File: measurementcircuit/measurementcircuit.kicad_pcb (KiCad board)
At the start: 2 copper layers, 174.5 x 220 mm, 81 parts, among them J1 Conn_01x02, J10 Conn_01x02, J11 Conn_01x02, J12 Conn_01x02, J13 250-108/000-006, J15 Conn_01x02, J16 Conn_01x02, J17 250-116/000-012, J18 2604-3102, J19 2604-3102, J2 Conn_01x02, J20 2604-3102, J21 Conn_01x02, J22 Conn_01x02, J23 Conn_01x02, J24 Conn_01x02, J25 Conn_01x02, J26 Conn_01x02, J27 Conn_01x02, J28 Conn_01x02, J29 Conn_01x02, J3 2604-3102, J30 Conn_01x02, J31 Conn_01x02, J32 Conn_01x02, J33 Conn_01x02, J34 Conn_01x02, J35 Conn_01x02, J36 Conn_01x02, J37 Conn_01x02, J38 Conn_01x02, J39 Conn_01x02, J4 2604-3102, J40 Conn_01x02, J41 Conn_01x02, J42 Conn_01x02, J5 2604-3102, J6 2604-3102, J7 2604-3102, J8 Conn_01x02, J9 Conn_01x02

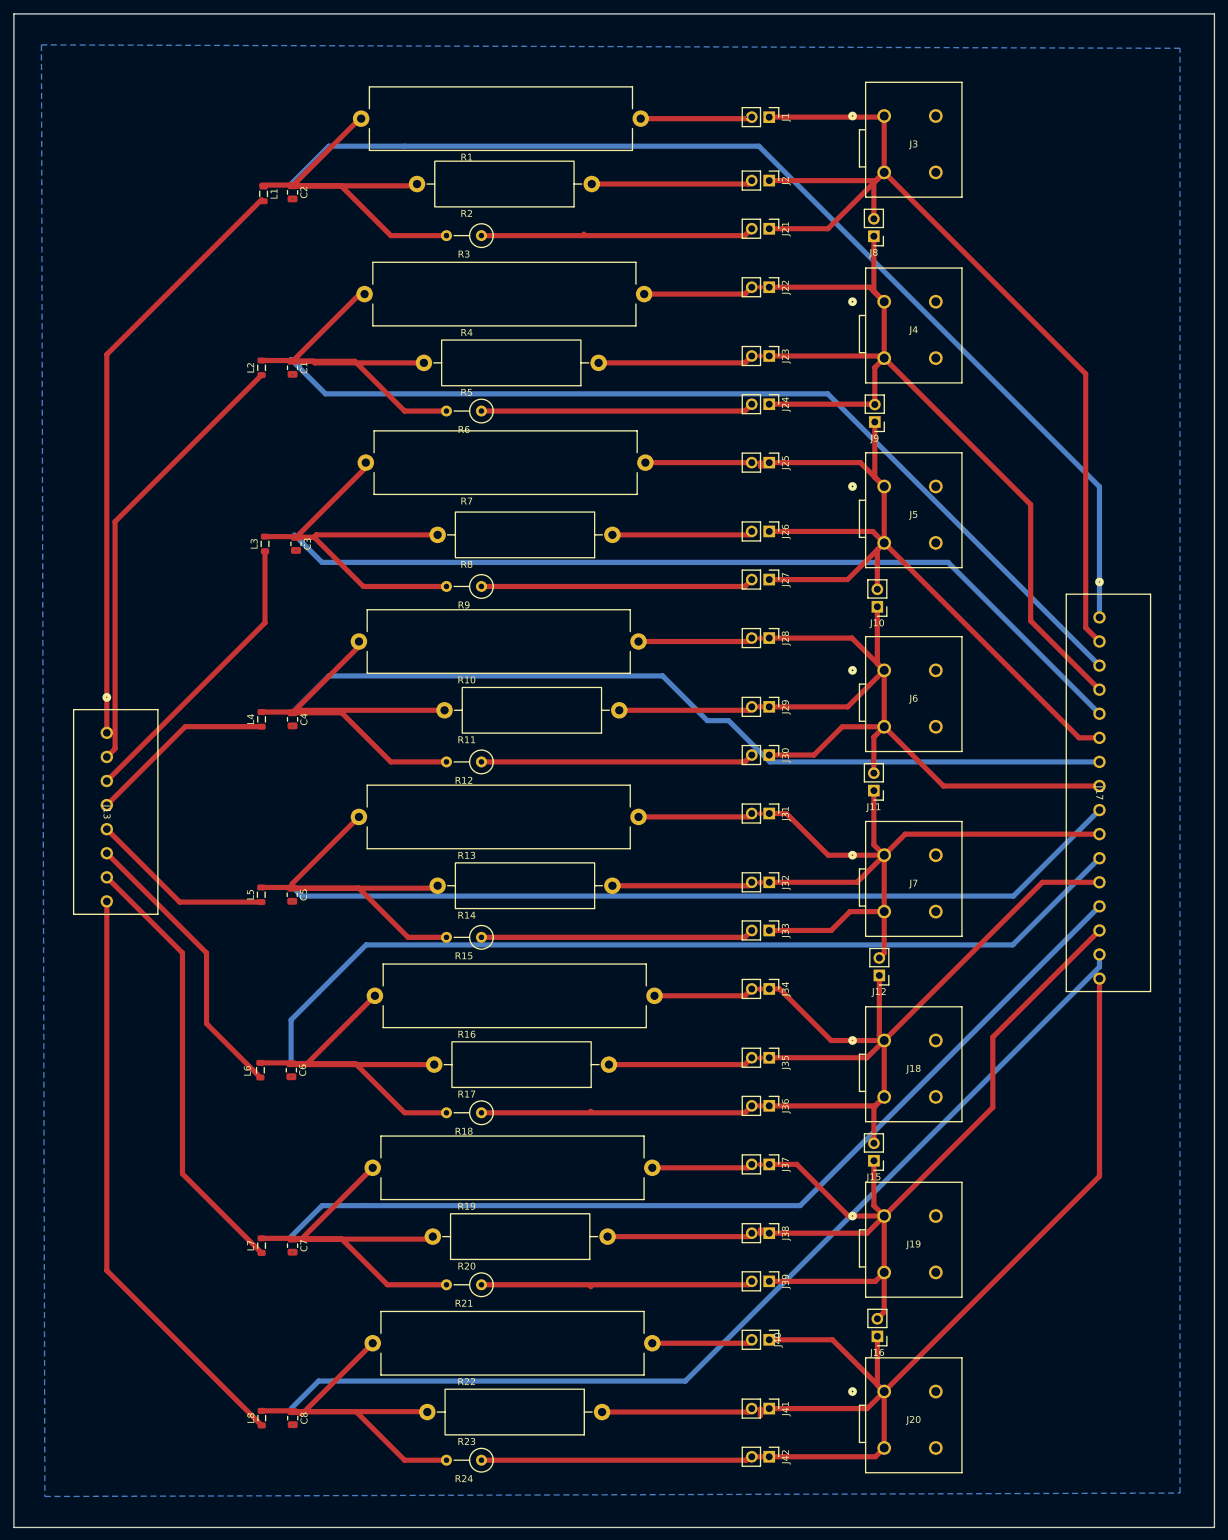
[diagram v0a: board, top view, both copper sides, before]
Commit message: First Redesign Changes
Switch to 4-layer PCB with inner copper layers as ground layers for top and bottom. Add holes for standoffs. Clockwise orientation of schematic to accommodate double the channels.
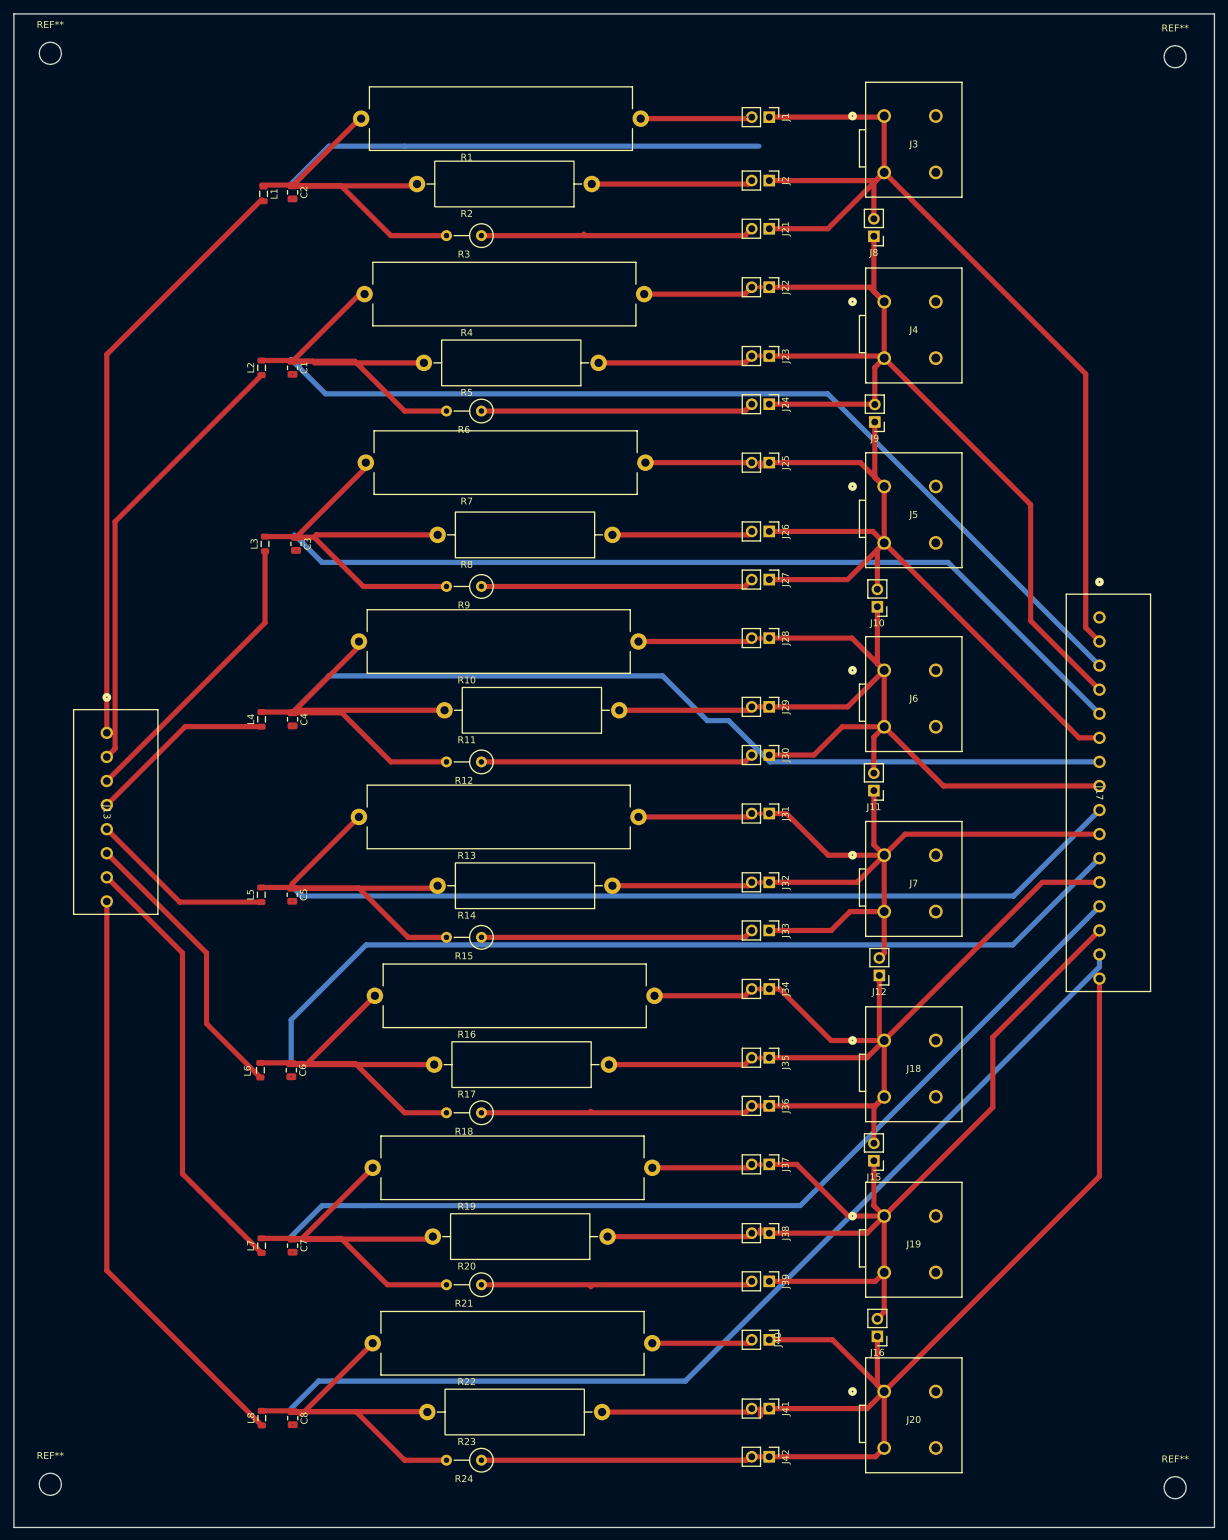
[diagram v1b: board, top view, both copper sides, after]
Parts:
- added REF**: MountingHole_3.2mm_M3, MountingHole:MountingHole_3.2mm_M3, F.Cu at (-26.5, 135.0)
- added REF**: MountingHole_3.2mm_M3, MountingHole:MountingHole_3.2mm_M3, F.Cu at (-26.5, -73.0)
- added REF**: MountingHole_3.2mm_M3, MountingHole:MountingHole_3.2mm_M3, F.Cu at (-190.0, -73.5)
- added REF**: MountingHole_3.2mm_M3, MountingHole:MountingHole_3.2mm_M3, F.Cu at (-190.0, 134.5)
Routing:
- net Net-(C2-Pad1): track 221.6 -> 132.6 mm
- added copper zone on In1.Cu, net GND
- added copper zone on In2.Cu, net GND
- removed copper zone on B.Cu, net GND
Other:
- copper layers 2 -> 4

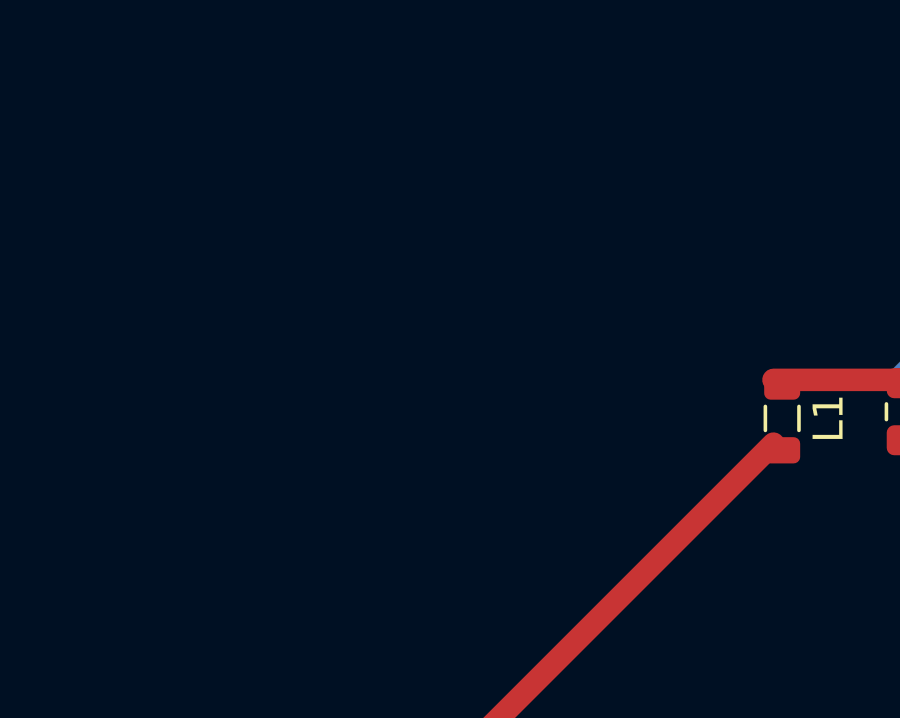
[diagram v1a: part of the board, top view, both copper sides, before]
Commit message: Redesign Work - Symbols, Schematic Overhaul
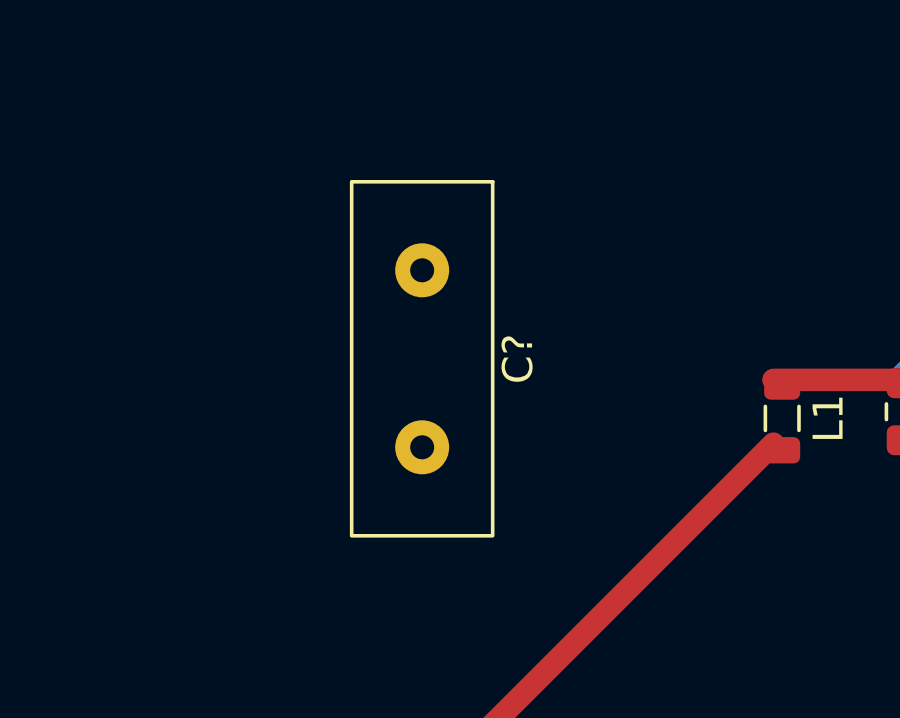
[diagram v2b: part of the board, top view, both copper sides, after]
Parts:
- added C?: 10pF, 10pF_Capacitor_Custom:C_Disc_Radial_P5.90mm_W4.3mm_L11.4mm_Placeholder, F.Cu at (-171.0, -58.0)
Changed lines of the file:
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@@
 		)
+	)
+	(footprint "10pF_Capacitor_Custom:C_Disc_Radial_P5.90mm_W4.3mm_L11.4mm_Placeholder"
+		(layer "F.Cu")
+		(at -171 -58 -90)
+		(descr "Placeholder: Cornell Dubilier CD17 series style mica cap, THT, 5.90mm pitch, body ~11.4x4.3mm")
+		(tags "capacitor THT radial mica placeholder P5.90mm")
+		(property "Reference" "C?"
+			(at 2.95 -3.2 90)
+			(layer "F.SilkS")
+			(effects
+				(font
+					(size 1 1)
+					(thickness 0.15)
+				)
+			)
+		)
+		(property "Value" "10pF"
+			(at 2.95 3.2 90)
+			(layer "F.Fab")
+			(effects
+				(font
+					(size 1 1)
+					(thickness 0.15)
+				)
+			)
+		)
+		(property "Datasheet" ""
+			(at 0 0 90)
+			(layer "F.Fab")
+			(hide yes)
+			(effects
+				(font
+					(size 1.27 1.27)
+					(thickness 0.15)
+				)
+			)
+		)
+		(property "Description" ""
+			(at 0 0 90)
+			(layer "F.Fab")
+			(hide yes)
+			(effects
+				(font
+					(size 1.27 1.27)
+					(thickness 0.15)
+				)
+			)
+		)
+		(attr through_hole)
+		(fp_rect
+			(start -2.95 -2.35)
+			(end 8.85 2.35)
+			(stroke
+				(width 0.12)
+				(type solid)
+			)
+			(fill no)
+			(layer "F.SilkS")
+		)
+		(fp_rect
+			(start -3.45 -2.85)
+			(end 9.35 2.85)
+			(stroke
+				(width 0.05)
+				(type solid)
+			)
+			(fill no)
+			(layer "F.CrtYd")
+		)
+		(fp_rect
+			(start -2.75 -2.15)
+			(end 8.65 2.15)
+			(stroke
+				(width 0.1)
+				(type solid)
+			)
+			(fill no)
+			(layer "F.Fab")
+		)
+		(fp_text user "${REFERENCE}"
+			(at 2.95 0 90)
+			(layer "F.Fab")
+			(effects
+				(font
+					(size 1 1)
+					(thickness 0.12)
+				)
+			)
+		)
+		(pad "1" thru_hole circle
+			(at 0 0 270)
+			(size 1.8 1.8)
+			(drill 0.8)
+			(layers "*.Cu" "*.Mask")
+			(remove_unused_layers no)
+		)
+		(pad "2" thru_hole circle
+			(at 5.9 0 270)
+			(size 1.8 1.8)
+			(drill 0.8)
+			(layers "*.Cu" "*.Mask")
+			(remove_unused_layers no)
+		)
+		(embedded_fonts no)
 	)
 	(footprint "Resistor_THT:R_Axial_Power_L20.0mm_W6.4mm_P25.40mm"

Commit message: Figured out Bottom layer placement, some footprint changes
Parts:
- removed C?: 10pF, 10pF_Capacitor_Custom:C_Disc_Radial_P5.90mm_W4.3mm_L11.4mm_Placeholder
- removed REF** (x4): MountingHole_3.2mm_M3, MountingHole:MountingHole_3.2mm_M3
- added C11: 10pF, Capacitor_SMD:C_0805_2012Metric, B.Cu at (48.4, -4.12)
- added C12: 10pF, Capacitor_SMD:C_0805_2012Metric, B.Cu at (48.4, -1.11)
- added C13: 10pF, Capacitor_SMD:C_0805_2012Metric, B.Cu at (48.4, 1.90)
- added C14: 10pF, Capacitor_SMD:C_0805_2012Metric, B.Cu at (48.4, 4.91)
- added C15: 10pF, Capacitor_SMD:C_0805_2012Metric, B.Cu at (48.4, 7.92)
- added C16: 10pF, Capacitor_SMD:C_0805_2012Metric, B.Cu at (48.4, 10.9)
- added C18: 10pF, Capacitor_SMD:C_0805_2012Metric, B.Cu at (48.4, 13.9)
- added J47: Conn_01x02, Connector_PinHeader_2.54mm:PinHeader_1x02_P2.54mm_Vertical, B.Cu at (80.5, -3.33)
- added J48: Conn_01x02, Connector_PinHeader_2.54mm:PinHeader_1x02_P2.54mm_Vertical, B.Cu at (75.9, -3.33)
- added J49: Conn_01x02, Connector_PinHeader_2.54mm:PinHeader_1x02_P2.54mm_Vertical, B.Cu at (71.3, -3.33)
- added J51: Conn_01x02, Connector_PinHeader_2.54mm:PinHeader_1x02_P2.54mm_Vertical, B.Cu at (66.7, -3.33)
- added J52: Conn_01x02, Connector_PinHeader_2.54mm:PinHeader_1x02_P2.54mm_Vertical, B.Cu at (62.1, -3.33)
- added J53: Conn_01x02, Connector_PinHeader_2.54mm:PinHeader_1x02_P2.54mm_Vertical, B.Cu at (57.5, -3.33)
- added J54: Conn_01x02, Connector_PinHeader_2.54mm:PinHeader_1x02_P2.54mm_Vertical, B.Cu at (80.5, 3.81)
- added J56: Conn_01x02, Connector_PinHeader_2.54mm:PinHeader_1x02_P2.54mm_Vertical, B.Cu at (75.9, 3.81)
- added J57: Conn_01x02, Connector_PinHeader_2.54mm:PinHeader_1x02_P2.54mm_Vertical, B.Cu at (71.3, 3.81)
- added J58: Conn_01x02, Connector_PinHeader_2.54mm:PinHeader_1x02_P2.54mm_Vertical, B.Cu at (66.7, 3.81)
- added J59: Conn_01x02, Connector_PinHeader_2.54mm:PinHeader_1x02_P2.54mm_Vertical, B.Cu at (62.1, 3.81)
- added J62: Conn_01x02, Connector_PinHeader_2.54mm:PinHeader_1x02_P2.54mm_Vertical, B.Cu at (57.5, 3.81)
- added J63: Conn_01x02, Connector_PinHeader_2.54mm:PinHeader_1x02_P2.54mm_Vertical, B.Cu at (80.5, 10.9)
- added J64: Conn_01x02, Connector_PinHeader_2.54mm:PinHeader_1x02_P2.54mm_Vertical, B.Cu at (75.9, 10.9)
- added J65: Conn_01x02, Connector_PinHeader_2.54mm:PinHeader_1x02_P2.54mm_Vertical, B.Cu at (71.3, 10.9)
- added J67: Conn_01x02, Connector_PinHeader_2.54mm:PinHeader_1x02_P2.54mm_Vertical, B.Cu at (66.7, 10.9)
- added J68: Conn_01x02, Connector_PinHeader_2.54mm:PinHeader_1x02_P2.54mm_Vertical, B.Cu at (62.1, 10.9)
- added J69: Conn_01x02, Connector_PinHeader_2.54mm:PinHeader_1x02_P2.54mm_Vertical, B.Cu at (57.5, 10.9)
- added J70: Conn_01x02, Connector_PinHeader_2.54mm:PinHeader_1x02_P2.54mm_Vertical, B.Cu at (80.5, 18.1)
- added J72: Conn_01x02, Connector_PinHeader_2.54mm:PinHeader_1x02_P2.54mm_Vertical, B.Cu at (75.9, 18.1)
- added J73: Conn_01x02, Connector_PinHeader_2.54mm:PinHeader_1x02_P2.54mm_Vertical, B.Cu at (71.3, 18.1)
- added J74: Conn_01x02, Connector_PinHeader_2.54mm:PinHeader_1x02_P2.54mm_Vertical, B.Cu at (66.7, 18.1)
- added J75: Conn_01x02, Connector_PinHeader_2.54mm:PinHeader_1x02_P2.54mm_Vertical, B.Cu at (62.1, 18.1)
- added J77: Conn_01x02, Connector_PinHeader_2.54mm:PinHeader_1x02_P2.54mm_Vertical, B.Cu at (57.5, 18.1)
- added J78: Conn_01x02, Connector_PinHeader_2.54mm:PinHeader_1x02_P2.54mm_Vertical, B.Cu at (80.5, 25.2)
- added J79: Conn_01x02, Connector_PinHeader_2.54mm:PinHeader_1x02_P2.54mm_Vertical, B.Cu at (75.9, 25.2)
- added J80: Conn_01x02, Connector_PinHeader_2.54mm:PinHeader_1x02_P2.54mm_Vertical, B.Cu at (71.3, 25.2)
- added J82: Conn_01x02, Connector_PinHeader_2.54mm:PinHeader_1x02_P2.54mm_Vertical, B.Cu at (66.7, 25.2)
- added J83: Conn_01x02, Connector_PinHeader_2.54mm:PinHeader_1x02_P2.54mm_Vertical, B.Cu at (62.1, 25.2)
- added J84: Conn_01x02, Connector_PinHeader_2.54mm:PinHeader_1x02_P2.54mm_Vertical, B.Cu at (57.5, 25.2)
- added L10: 56μH, Inductor_SMD:L_0805_2012Metric, B.Cu at (52.9, -1.50)
- added L11: 56μH, Inductor_SMD:L_0805_2012Metric, B.Cu at (52.9, 1.25)
- added L12: 56μH, Inductor_SMD:L_0805_2012Metric, B.Cu at (52.9, 4.00)
- added L13: 56μH, Inductor_SMD:L_0805_2012Metric, B.Cu at (52.9, 6.75)
- added L14: 56μH, Inductor_SMD:L_0805_2012Metric, B.Cu at (52.9, 9.49)
- added L15: 56μH, Inductor_SMD:L_0805_2012Metric, B.Cu at (52.9, 12.2)
- added L16: 56μH, Inductor_SMD:L_0805_2012Metric, B.Cu at (52.9, 15.0)
- added L9: 56μH, Inductor_SMD:L_0805_2012Metric, B.Cu at (52.9, -4.25)
- added R25: 10 Ohm, Resistor_THT:R_Axial_Power_L38.0mm_W9.0mm_P40.64mm, B.Cu at (4.64, -64.0)
- added R26: 50 Ohm, Resistor_THT:R_Axial_Power_L20.0mm_W6.4mm_P25.40mm, B.Cu at (80.8, -65.3)
- added R27: 500 Ohm, Resistor_THT:R_Axial_DIN0309_L9.0mm_D3.2mm_P5.08mm_Vertical, B.Cu at (51.0, -66.9)
- added R28: 10 Ohm, Resistor_THT:R_Axial_Power_L38.0mm_W9.0mm_P40.64mm, B.Cu at (45.3, -53.4)
- added R29: 50 Ohm, Resistor_THT:R_Axial_Power_L20.0mm_W6.4mm_P25.40mm, B.Cu at (80.8, -57.3)
- added R30: 500 Ohm, Resistor_THT:R_Axial_DIN0309_L9.0mm_D3.2mm_P5.08mm_Vertical, B.Cu at (51.0, -62.1)
- added R31: 10 Ohm, Resistor_THT:R_Axial_Power_L38.0mm_W9.0mm_P40.64mm, B.Cu at (45.3, -42.9)
- added R32: 50 Ohm, Resistor_THT:R_Axial_Power_L20.0mm_W6.4mm_P25.40mm, B.Cu at (80.8, -49.4)
- added R33: 500 Ohm, Resistor_THT:R_Axial_DIN0309_L9.0mm_D3.2mm_P5.08mm_Vertical, B.Cu at (51.0, -57.4)
- added R34: 10 Ohm, Resistor_THT:R_Axial_Power_L38.0mm_W9.0mm_P40.64mm, B.Cu at (45.3, -32.3)
- added R35: 50 Ohm, Resistor_THT:R_Axial_Power_L20.0mm_W6.4mm_P25.40mm, B.Cu at (80.8, -41.4)
- added R36: 500 Ohm, Resistor_THT:R_Axial_DIN0309_L9.0mm_D3.2mm_P5.08mm_Vertical, B.Cu at (51.0, -52.6)
- added R37: 10 Ohm, Resistor_THT:R_Axial_Power_L38.0mm_W9.0mm_P40.64mm, B.Cu at (45.3, -21.8)
- added R38: 50 Ohm, Resistor_THT:R_Axial_Power_L20.0mm_W6.4mm_P25.40mm, B.Cu at (80.8, -33.5)
- added R39: 500 Ohm, Resistor_THT:R_Axial_DIN0309_L9.0mm_D3.2mm_P5.08mm_Vertical, B.Cu at (51.0, -47.9)
- added R40: 10 Ohm, Resistor_THT:R_Axial_Power_L38.0mm_W9.0mm_P40.64mm, B.Cu at (45.3, -11.2)
- added R41: 50 Ohm, Resistor_THT:R_Axial_Power_L20.0mm_W6.4mm_P25.40mm, B.Cu at (80.8, -25.5)
- added R42: 500 Ohm, Resistor_THT:R_Axial_DIN0309_L9.0mm_D3.2mm_P5.08mm_Vertical, B.Cu at (51.0, -43.1)
- added R43: 10 Ohm, Resistor_THT:R_Axial_Power_L38.0mm_W9.0mm_P40.64mm, B.Cu at (45.3, -0.66)
- added R44: 50 Ohm, Resistor_THT:R_Axial_Power_L20.0mm_W6.4mm_P25.40mm, B.Cu at (80.8, -17.6)
- added R45: 500 Ohm, Resistor_THT:R_Axial_DIN0309_L9.0mm_D3.2mm_P5.08mm_Vertical, B.Cu at (51.0, -38.4)
- added R46: 10 Ohm, Resistor_THT:R_Axial_Power_L38.0mm_W9.0mm_P40.64mm, B.Cu at (45.3, 9.89)
- added R47: 50 Ohm, Resistor_THT:R_Axial_Power_L20.0mm_W6.4mm_P25.40mm, B.Cu at (80.8, -9.61)
- added R48: 500 Ohm, Resistor_THT:R_Axial_DIN0309_L9.0mm_D3.2mm_P5.08mm_Vertical, B.Cu at (51.0, -33.6)
- J13: value 250-108/000-006 -> 2604-3102
- J17: value 250-116/000-012 -> Conn_01x02; footprint Senior_Design:CONN16_250-116&slash_000-012_WAG -> Connector_PinHeader_2.54mm:PinHeader_1x02_P2.54mm_Vertical
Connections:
- C1 pad 1: Net-(J22-Pin_1) -> Net-(J4-1_1)
- C4 pad 1: Net-(J10-Pin_1) -> Net-(C4-Pad1)
- J13 pad 1: Net-(J13-Pad1) -> Net-(J13-1_1)
- J13 pad 2: Net-(J13-Pad2) -> Net-(J13-1_1)
- J13 pad 3: Net-(J13-Pad3) -> GND
- J13 pad 4: Net-(J13-Pad4) -> GND
- J13 pad 5: Net-(J13-Pad5) -> (no net)
- J13 pad 6: Net-(J13-Pad6) -> (no net)
- J13 pad 7: Net-(J13-Pad7) -> (no net)
- J13 pad 8: Net-(J13-Pad8) -> (no net)
- J17 pad 1: Net-(C2-Pad1) -> Net-(J13-1_1)
- J17 pad 2: Net-(J1-Pin_1) -> Net-(J17-Pin_2)
- J4 pad 1: Net-(J22-Pin_1) -> Net-(J4-1_1)
- J4 pad 2: Net-(J22-Pin_1) -> Net-(J4-1_1)
- J9 pad 2: Net-(J22-Pin_1) -> Net-(J4-1_1)
- L1 pad 1: Net-(J13-Pad1) -> Net-(J46-8_1)
- L2 pad 1: Net-(J13-Pad2) -> Net-(J46-7_1)
- L2 pad 2: Net-(J22-Pin_1) -> Net-(J4-1_1)
- L3 pad 1: Net-(J13-Pad3) -> Net-(J46-6_1)
- L4 pad 1: Net-(J13-Pad4) -> Net-(J46-5_1)
- L4 pad 2: Net-(J10-Pin_1) -> Net-(C4-Pad1)
- L5 pad 1: Net-(J13-Pad5) -> Net-(J46-4_1)
- L6 pad 1: Net-(J13-Pad6) -> Net-(J46-3_1)
- L7 pad 1: Net-(J13-Pad7) -> Net-(J46-2_1)
- L8 pad 1: Net-(J13-Pad8) -> Net-(J46-1_1)
- R10 pad 2: Net-(J10-Pin_1) -> Net-(C4-Pad1)
- R11 pad 2: Net-(J10-Pin_1) -> Net-(C4-Pad1)
- R12 pad 2: Net-(J10-Pin_1) -> Net-(C4-Pad1)
- R4 pad 2: Net-(J22-Pin_1) -> Net-(J4-1_1)
- R5 pad 2: Net-(J22-Pin_1) -> Net-(J4-1_1)
- R6 pad 2: Net-(J22-Pin_1) -> Net-(J4-1_1)
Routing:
- net Net-(C2-Pad1): track 132.6 -> 284.3 mm
- net Net-(J13-Pad1): track 86.8 -> 0.00 mm
- net Net-(J46-1_1): track 0.00 -> 85.5 mm
- net Net-(J13-Pad8): track 85.5 -> 0.00 mm
- net GND: track 0.00 -> 70.1 mm
- net Net-(J10-Pin_1): track 306.9 -> 240.4 mm
- net Net-(C4-Pad1): track 0.00 -> 66.5 mm
- net Net-(J13-Pad2): track 64.8 -> 0.00 mm
- net Net-(J46-2_1): track 0.00 -> 63.9 mm
- net Net-(J13-Pad7): track 63.9 -> 0.00 mm
- net Net-(J22-Pin_1): track 336.2 -> 272.5 mm
- net Net-(J4-1_1): track 0.00 -> 63.6 mm
- net Net-(J13-Pad3): track 42.9 -> 0.00 mm
- net Net-(J46-3_1): track 0.00 -> 41.8 mm
- net Net-(J13-Pad6): track 41.8 -> 0.00 mm
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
